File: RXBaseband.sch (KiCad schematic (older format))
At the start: 14 parts, among them U4 MCP6002-I/P, U5 MAX7413CPA+

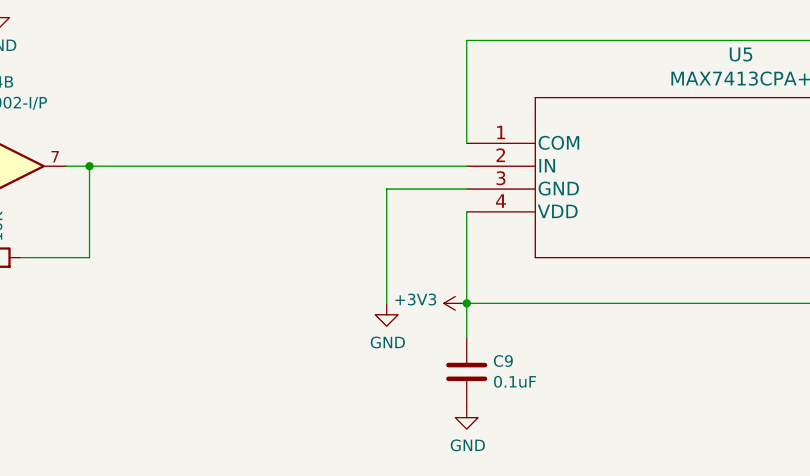
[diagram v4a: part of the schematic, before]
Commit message: increased passives to 0805. preliminary layout.
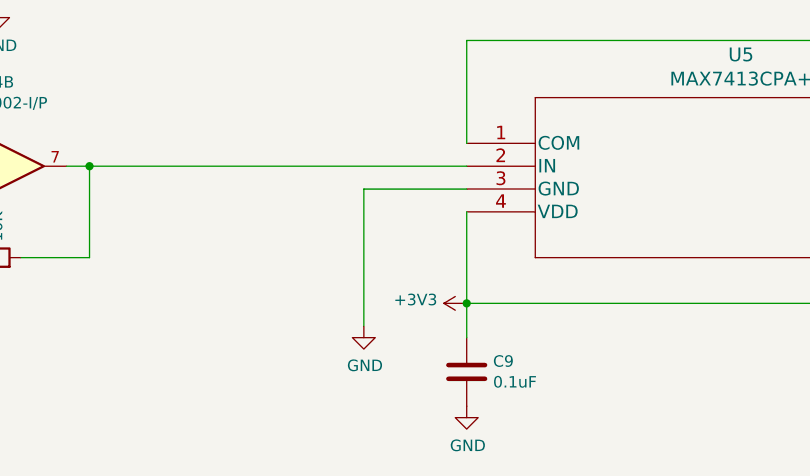
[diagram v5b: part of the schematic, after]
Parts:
- C10, C11, C8, C9: footprint Capacitor_SMD:C_0603_1608Metric -> Capacitor_SMD:C_0805_2012Metric_Pad1.18x1.45mm_HandSolder
- R10, R11, R12, R13, R14, R15, R16: footprint Resistor_SMD:R_0603_1608Metric -> Resistor_SMD:R_0805_2012Metric_Pad1.20x1.40mm_HandSolder
- RV3: footprint (none) -> Potentiometer_SMD:Potentiometer_Bourns_3361P_Vertical
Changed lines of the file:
@@
 F 0 "R13" H 8570 4196 50  0000 L CNN
 F 1 "10K" H 8570 4105 50  0000 L CNN
-F 2 "Resistor_SMD:R_0603_1608Metric" V 8430 4150 50  0001 C CNN
+F 2 "Resistor_SMD:R_0805_2012Metric_Pad1.20x1.40mm_HandSolder" V 8430 4150 50  0001 C CNN
 F 3 "~" H 8500 4150 50  0001 C CNN
 	1    8500 4150
@@
 F 0 "R11" H 1720 4396 50  0000 L CNN
 F 1 "22K" H 1720 4305 50  0000 L CNN
-F 2 "Resistor_SMD:R_0603_1608Metric" V 1580 4350 50  0001 C CNN
+F 2 "Resistor_SMD:R_0805_2012Metric_Pad1.20x1.40mm_HandSolder" V 1580 4350 50  0001 C CNN
 F 3 "~" H 1650 4350 50  0001 C CNN
 	1    1650 4350
@@
 F 0 "R14" V 8293 4500 50  0000 C CNN
 F 1 "10K" V 8384 4500 50  0000 C CNN
-F 2 "Resistor_SMD:R_0603_1608Metric" V 8430 4500 50  0001 C CNN
+F 2 "Resistor_SMD:R_0805_2012Metric_Pad1.20x1.40mm_HandSolder" V 8430 4500 50  0001 C CNN
 F 3 "~" H 8500 4500 50  0001 C CNN
 	1    8500 4500
@@
 F 0 "R15" V 8793 4950 50  0000 C CNN
 F 1 "100R" V 8884 4950 50  0000 C CNN
-F 2 "Resistor_SMD:R_0603_1608Metric" V 8930 4950 50  0001 C CNN
+F 2 "Resistor_SMD:R_0805_2012Metric_Pad1.20x1.40mm_HandSolder" V 8930 4950 50  0001 C CNN
 F 3 "~" H 9000 4950 50  0001 C CNN
 	1    9000 4950
@@
 F 0 "RV3" H 9331 4904 50  0000 R CNN
 F 1 "4K7" H 9331 4995 50  0000 R CNN
-F 2 "" H 9400 4950 50  0001 C CNN
+F 2 "Potentiometer_SMD:Potentiometer_Bourns_3361P_Vertical" H 9400 4950 50  0001 C CNN
 F 3 "~" H 9400 4950 50  0001 C CNN
 	1    9400 4950
@@
 F 0 "C11" V 8545 3900 50  0000 C CNN
 F 1 "10u" V 8636 3900 50  0000 C CNN
-F 2 "Capacitor_SMD:C_0603_1608Metric" H 8838 3750 50  0001 C CNN
+F 2 "Capacitor_SMD:C_0805_2012Metric_Pad1.18x1.45mm_HandSolder" H 8838 3750 50  0001 C CNN
 F 3 "~" H 8800 3900 50  0001 C CNN
 	1    8800 3900
@@
 F 0 "R10" H 1720 3696 50  0000 L CNN
 F 1 "22K" H 1720 3605 50  0000 L CNN
-F 2 "Resistor_SMD:R_0603_1608Metric" V 1580 3650 50  0001 C CNN
+F 2 "Resistor_SMD:R_0805_2012Metric_Pad1.20x1.40mm_HandSolder" V 1580 3650 50  0001 C CNN
 F 3 "~" H 1650 3650 50  0001 C CNN
 	1    1650 3650
@@
 F 0 "R12" H 2320 4546 50  0000 L CNN
 F 1 "10K" H 2320 4455 50  0000 L CNN
-F 2 "Resistor_SMD:R_0603_1608Metric" V 2180 4500 50  0001 C CNN
+F 2 "Resistor_SMD:R_0805_2012Metric_Pad1.20x1.40mm_HandSolder" V 2180 4500 50  0001 C CNN
 F 3 "~" H 2250 4500 50  0001 C CNN
 	1    2250 4500
@@
 F 0 "R16" H 9920 4446 50  0000 L CNN
 F 1 "33K" H 9920 4355 50  0000 L CNN
-F 2 "Resistor_SMD:R_0603_1608Metric" V 9780 4400 50  0001 C CNN
+F 2 "Resistor_SMD:R_0805_2012Metric_Pad1.20x1.40mm_HandSolder" V 9780 4400 50  0001 C CNN
 F 3 "~" H 9850 4400 50  0001 C CNN
 	1    9850 4400
@@
 F 0 "C8" V 1795 3100 50  0000 C CNN
 F 1 "10u" V 1886 3100 50  0000 C CNN
-F 2 "Capacitor_SMD:C_0603_1608Metric" H 2088 2950 50  0001 C CNN
+F 2 "Capacitor_SMD:C_0805_2012Metric_Pad1.18x1.45mm_HandSolder" H 2088 2950 50  0001 C CNN
 F 3 "~" H 2050 3100 50  0001 C CNN
 	1    2050 3100
@@
 F 0 "C9" H 4465 5046 50  0000 L CNN
 F 1 "0.1uF" H 4465 4955 50  0000 L CNN
-F 2 "Capacitor_SMD:C_0603_1608Metric" H 4388 4850 50  0001 C CNN
+F 2 "Capacitor_SMD:C_0805_2012Metric_Pad1.18x1.45mm_HandSolder" H 4388 4850 50  0001 C CNN
 F 3 "~" H 4350 5000 50  0001 C CNN
 	1    4350 5000
@@
 FLT_CLK
 Wire Wire Line
-	4350 4200 4000 4200
-Wire Wire Line
-	4000 4200 4000 4700
+	4350 4200 3900 4200
+Wire Wire Line
+	3900 4200 3900 4800
 $Comp
 L power:GND #PWR044
 U 1 1 605841CF
-P 4000 4700
-F 0 "#PWR044" H 4000 4450 50  0001 C CNN
-F 1 "GND" H 4005 4527 50  0000 C CNN
-F 2 "" H 4000 4700 50  0001 C CNN
-F 3 "" H 4000 4700 50  0001 C CNN
-	1    4000 4700
+P 3900 4800
+F 0 "#PWR044" H 3900 4550 50  0001 C CNN
+F 1 "GND" H 3905 4627 50  0000 C CNN
+F 2 "" H 3900 4800 50  0001 C CNN
+F 3 "" H 3900 4800 50  0001 C CNN
+	1    3900 4800
 	1    0    0    -1
 $EndComp
@@
 F 0 "C10" V 7048 3550 50  0000 C CNN
 F 1 "0.22uF" V 7139 3550 50  0000 C CNN
-F 2 "Capacitor_SMD:C_0603_1608Metric" H 7338 3400 50  0001 C CNN
+F 2 "Capacitor_SMD:C_0805_2012Metric_Pad1.18x1.45mm_HandSolder" H 7338 3400 50  0001 C CNN
 F 3 "~" H 7300 3550 50  0001 C CNN
 	1    7300 3550

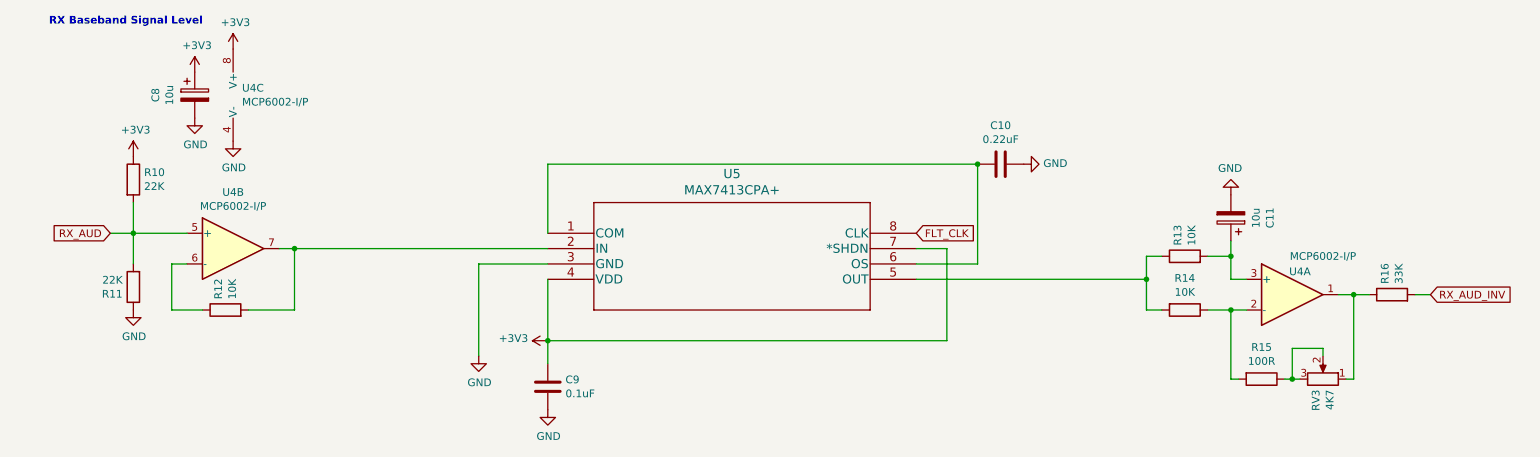
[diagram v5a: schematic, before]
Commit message: part and footprint updates, routing
updated parts and footprints for header and transistors. updated layout. most routing is complete pending changes to schematic.
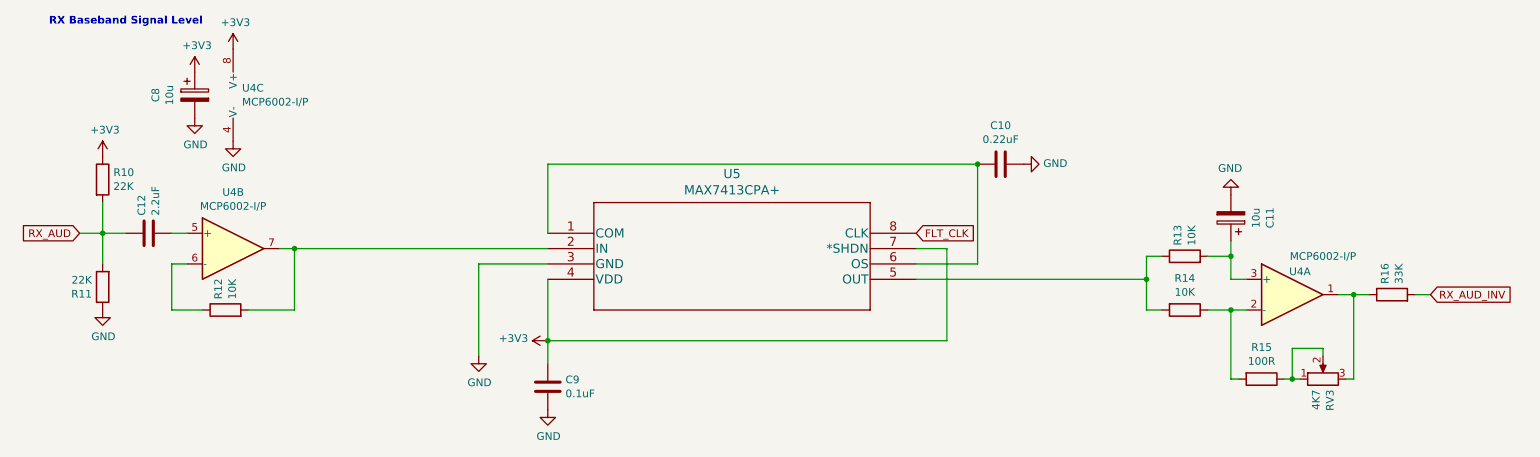
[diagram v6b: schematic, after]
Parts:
- added C12: 2.2uF, Capacitor_SMD:C_0805_2012Metric_Pad1.18x1.45mm_HandSolder, symbol Device:C
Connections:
- net RX_AUD: now also C12.1; no longer U4.5 (+)
- net at R16.1, U4.1: now also RV3.3; no longer RV3.1
- net at R15.1, RV3.2: now also RV3.1; no longer RV3.3
- new net: C12.2, U4.5 (+)
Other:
- moved on the sheet: R10, R11
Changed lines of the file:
@@
 L Device:R R11
 U 1 1 60561DA6
-P 1650 4350
-F 0 "R11" H 1720 4396 50  0000 L CNN
-F 1 "22K" H 1720 4305 50  0000 L CNN
-F 2 "Resistor_SMD:R_0805_2012Metric_Pad1.20x1.40mm_HandSolder" V 1580 4350 50  0001 C CNN
-F 3 "~" H 1650 4350 50  0001 C CNN
-	1    1650 4350
+P 1450 4350
+F 0 "R11" H 1520 4396 50  0000 L CNN
+F 1 "22K" H 1520 4305 50  0000 L CNN
+F 2 "Resistor_SMD:R_0805_2012Metric_Pad1.20x1.40mm_HandSolder" V 1380 4350 50  0001 C CNN
+F 3 "~" H 1450 4350 50  0001 C CNN
+	1    1450 4350
 	-1   0    0    1
 $EndComp
@@
 L power:GND #PWR039
 U 1 1 60561DAC
-P 1650 4500
-F 0 "#PWR039" H 1650 4250 50  0001 C CNN
-F 1 "GND" H 1655 4327 50  0000 C CNN
-F 2 "" H 1650 4500 50  0001 C CNN
-F 3 "" H 1650 4500 50  0001 C CNN
-	1    1650 4500
+P 1450 4500
+F 0 "#PWR039" H 1450 4250 50  0001 C CNN
+F 1 "GND" H 1455 4327 50  0000 C CNN
+F 2 "" H 1450 4500 50  0001 C CNN
+F 3 "" H 1450 4500 50  0001 C CNN
+	1    1450 4500
 	1    0    0    -1
 $EndComp
@@
 	0    1    1    0
 $EndComp
-Text GLabel 1500 4000 0    50   Input ~ 0
+Text GLabel 1300 4000 0    50   Input ~ 0
 RX_AUD
 $Comp
@@
 	0    1    1    0
 $EndComp
-$Comp
-L M17_GM300_RPi-rescue:R_POT-Device RV3
-U 1 1 60561DBF
-P 9400 4950
-F 0 "RV3" H 9331 4904 50  0000 R CNN
-F 1 "4K7" H 9331 4995 50  0000 R CNN
-F 2 "Potentiometer_SMD:Potentiometer_Bourns_3361P_Vertical" H 9400 4950 50  0001 C CNN
-F 3 "~" H 9400 4950 50  0001 C CNN
-	1    9400 4950
-	0    1    -1   0
-$EndComp
 Wire Wire Line
 	9600 4400 9700 4400
@@
 L Device:R R10
 U 1 1 60561DDD
-P 1650 3650
-F 0 "R10" H 1720 3696 50  0000 L CNN
-F 1 "22K" H 1720 3605 50  0000 L CNN
-F 2 "Resistor_SMD:R_0805_2012Metric_Pad1.20x1.40mm_HandSolder" V 1580 3650 50  0001 C CNN
-F 3 "~" H 1650 3650 50  0001 C CNN
-	1    1650 3650
+P 1450 3650
+F 0 "R10" H 1520 3696 50  0000 L CNN
+F 1 "22K" H 1520 3605 50  0000 L CNN
+F 2 "Resistor_SMD:R_0805_2012Metric_Pad1.20x1.40mm_HandSolder" V 1380 3650 50  0001 C CNN
+F 3 "~" H 1450 3650 50  0001 C CNN
+	1    1450 3650
 	1    0    0    -1
 $EndComp
@@
 L power:+3V3 #PWR038
 U 1 1 60561DE3
-P 1650 3500
-F 0 "#PWR038" H 1650 3350 50  0001 C CNN
-F 1 "+3V3" H 1665 3673 50  0000 C CNN
-F 2 "" H 1650 3500 50  0001 C CNN
-F 3 "" H 1650 3500 50  0001 C CNN
-	1    1650 3500
-	1    0    0    -1
-$EndComp
-Wire Wire Line
-	1650 3800 1650 4000
-Wire Wire Line
-	1500 4000 1650 4000
-Connection ~ 1650 4000
-Wire Wire Line
-	1650 4000 1650 4200
-Wire Wire Line
-	1650 4000 2000 4000
+P 1450 3500
+F 0 "#PWR038" H 1450 3350 50  0001 C CNN
+F 1 "+3V3" H 1465 3673 50  0000 C CNN
+F 2 "" H 1450 3500 50  0001 C CNN
+F 3 "" H 1450 3500 50  0001 C CNN
+	1    1450 3500
+	1    0    0    -1
+$EndComp
+Wire Wire Line
+	1450 3800 1450 4000
+Wire Wire Line
+	1300 4000 1450 4000
+Connection ~ 1450 4000
+Wire Wire Line
+	1450 4000 1450 4200
+Wire Wire Line
+	1450 4000 1600 4000
 $Comp
 L Device:R R12
@@
 Wire Wire Line
 	9550 4950 9600 4950
-Wire Wire Line
-	9400 4800 9400 4750
-Wire Wire Line
-	9400 4750 9200 4750
-Wire Wire Line
-	9200 4750 9200 4950
-Wire Wire Line
-	9200 4950 9250 4950
-Wire Wire Line
-	9200 4950 9150 4950
-Connection ~ 9200 4950
 Wire Wire Line
 	8800 4950 8850 4950
@@
 Wire Wire Line
 	2700 4100 4350 4100
+Wire Wire Line
+	1900 4000 2000 4000
+$Comp
+L Device:C C12
+U 1 1 6074A4AD
+P 1750 4000
+F 0 "C12" H 1865 4046 50  0000 L CNN
+F 1 "2.2uF" H 1865 3955 50  0000 L CNN
+F 2 "Capacitor_SMD:C_0805_2012Metric_Pad1.18x1.45mm_HandSolder" H 1788 3850 50  0001 C CNN
+F 3 "~" H 1750 4000 50  0001 C CNN
+	1    1750 4000
+	0    -1   -1   0
+$EndComp
+$Comp
+L M17_GM300_RPi-rescue:R_POT-Device RV3
+U 1 1 60561DBF
+P 9400 4950
+F 0 "RV3" H 9331 4904 50  0000 R CNN
+F 1 "4K7" H 9331 4995 50  0000 R CNN
+F 2 "Potentiometer_SMD:Potentiometer_Bourns_3361P_Vertical" H 9400 4950 50  0001 C CNN
+F 3 "~" H 9400 4950 50  0001 C CNN
+	1    9400 4950
+	0    -1   -1   0
+$EndComp
+Wire Wire Line
+	9400 4800 9400 4750
+Wire Wire Line
+	9400 4750 9200 4750
+Wire Wire Line
+	9200 4750 9200 4950
+Wire Wire Line
+	9200 4950 9150 4950
+Wire Wire Line
+	9250 4950 9200 4950
+Connection ~ 9200 4950
 $EndSCHEMATC
